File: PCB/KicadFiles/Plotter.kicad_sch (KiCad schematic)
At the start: 0 parts

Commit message: TMC2209 in Kicad
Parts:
- added U1: TMC2209-V1.2_Bigtreetech, Footprints:TMC2209-V1.2 Bigtreetech, symbol Symbols:TMC2209-V1.2_Bigtreetech
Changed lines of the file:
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@@
 (kicad_sch (version 20211123) (generator eeschema)
   (paper "A4")
+  (symbol (lib_id "Symbols:TMC2209-V1.2_Bigtreetech") (at 121.92 92.71 0) (unit 1)
+    (in_bom yes) (on_board yes) (fields_autoplaced)
+    (property "Reference" "U1" (id 0) (at 88.9 110.4899 0)
+      (effects (font (size 1.27 1.27)) (justify left))
+    )
+    (property "Value" "TMC2209-V1.2_Bigtreetech" (id 1) (at 88.9 113.0299 0)
+      (effects (font (size 1.27 1.27)) (justify left))
+    )
+    (property "Footprint" "Footprints:TMC2209-V1.2 Bigtreetech" (id 2) (at 87.63 78.74 0)
+      (effects (font (size 1.27 1.27)) hide)
+    )
+    (property "Datasheet" "https://github.com/bigtreetech/BIGTREETECH-TMC2209-V1.2/raw/master/Schematic/TMC2209-V1.2.pdf" (id 3) (at 92.71 67.31 0)
+      (effects (font (size 1.27 1.27)) hide)
+    )
+    (pin "1")
+    (pin "10")
+    (pin "11")
+    (pin "12")
+    (pin "13")
+    (pin "14")
+    (pin "15")
+    (pin "16")
+    (pin "17")
+    (pin "18")
+    (pin "2")
+    (pin "3")
+    (pin "4")
+    (pin "5")
+    (pin "6")
+    (pin "7")
+    (pin "8")
+    (pin "9")
+  )
   (sheet_instances
     (path "/" (page "1"))
   )
+  (symbol_instances
+    (path "/55d733b0-46c3-4709-8233-5c6162cfaae5"
+      (reference "U1") (unit 1) (value "TMC2209-V1.2_Bigtreetech") (footprint "Footprints:TMC2209-V1.2 Bigtreetech")
+    )
+  )
 )

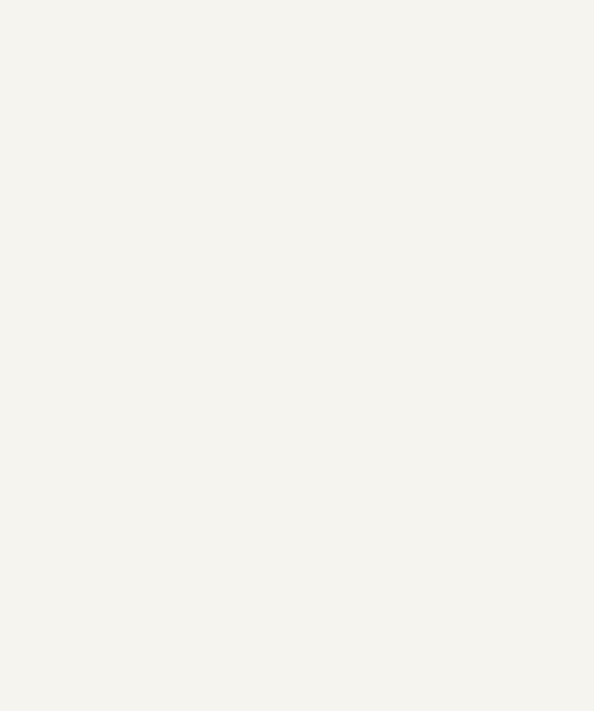
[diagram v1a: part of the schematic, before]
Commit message: stall detect lauft
https://github.com/teemuatlut/TMCStepper/issues/178
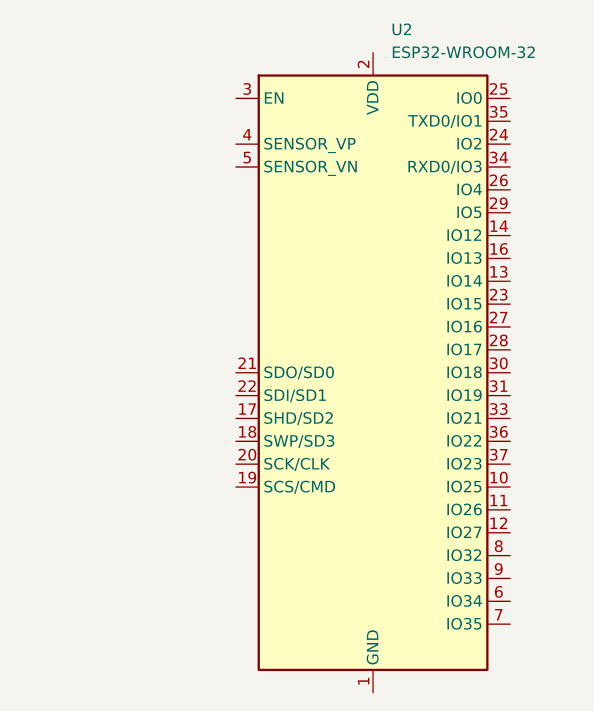
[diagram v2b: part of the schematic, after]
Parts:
- added U2: ESP32-WROOM-32, RF_Module:ESP32-WROOM-32, symbol RF_Module:ESP32-WROOM-32
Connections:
- new net: U2.1 (GND), U2.15 (GND), U2.38 (GND), U2.39 (GND)
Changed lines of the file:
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@@
+    (pin "9")
+  )
+  (symbol (lib_id "RF_Module:ESP32-WROOM-32") (at 176.53 106.68 0) (unit 1)
+    (in_bom yes) (on_board yes) (fields_autoplaced)
+    (property "Reference" "U2" (id 0) (at 178.5494 68.58 0)
+      (effects (font (size 1.27 1.27)) (justify left))
+    )
+    (property "Value" "ESP32-WROOM-32" (id 1) (at 178.5494 71.12 0)
+      (effects (font (size 1.27 1.27)) (justify left))
+    )
+    (property "Footprint" "RF_Module:ESP32-WROOM-32" (id 2) (at 176.53 144.78 0)
+      (effects (font (size 1.27 1.27)) hide)
+    )
+    (property "Datasheet" "https://www.espressif.com/sites/default/files/documentation/esp32-wroom-32_datasheet_en.pdf" (id 3) (at 168.91 105.41 0)
+      (effects (font (size 1.27 1.27)) hide)
+    )
+    (pin "1")
+    (pin "10")
+    (pin "11")
+    (pin "12")
+    (pin "13")
+    (pin "14")
+    (pin "15")
+    (pin "16")
+    (pin "17")
+    (pin "18")
+    (pin "19")
+    (pin "2")
+    (pin "20")
+    (pin "21")
+    (pin "22")
+    (pin "23")
+    (pin "24")
+    (pin "25")
+    (pin "26")
+    (pin "27")
+    (pin "28")
+    (pin "29")
+    (pin "3")
+    (pin "30")
+    (pin "31")
+    (pin "32")
+    (pin "33")
+    (pin "34")
+    (pin "35")
+    (pin "36")
+    (pin "37")
+    (pin "38")
+    (pin "39")
+    (pin "4")
+    (pin "5")
+    (pin "6")
+    (pin "7")
+    (pin "8")
     (pin "9")
   )
@@
       (reference "U1") (unit 1) (value "TMC2209-V1.2_Bigtreetech") (footprint "Footprints:TMC2209-V1.2 Bigtreetech")
     )
+    (path "/824942d7-4ef1-44b4-bd5a-14c81b4cd561"
+      (reference "U2") (unit 1) (value "ESP32-WROOM-32") (footprint "RF_Module:ESP32-WROOM-32")
+    )
   )

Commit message: schematic half way done
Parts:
- removed U1: TMC2209-V1.2_Bigtreetech, Footprints:TMC2209-V1.2 Bigtreetech, symbol Symbols:TMC2209-V1.2_Bigtreetech
- added C1, C2, C3, C6: 100u, Capacitor_SMD:CP_Elec_6.3x7.7, symbol Device:C_Polarized
- added C4, C5: C, Capacitor_SMD:C_0603_1608Metric, symbol Device:C
- added D1, D3, D4, D5: LED, LED_SMD:LED_0603_1608Metric, symbol Device:LED
- added D2: 10v, Package_TO_SOT_SMD:SOT-23, symbol Diode:BZX84Cxx
- added F1: Fuse, Fuse:Fuseholder_Cylinder-5x20mm_Schurter_0031_8201_Horizontal_Open, symbol Device:Fuse
- added H1, H2, H3, H4: MountingHole M3, MountingHole:MountingHole_3.2mm_M3_Pad_Via, symbol Mechanical:MountingHole_Pad
- added J1: JTAG, Connector_IDC:IDC-Header_2x10_P2.54mm_Vertical, symbol Connector_Generic:Conn_02x10_Odd_Even
- added J2: DBG_UART, Connector_JST:JST_XH_B3B-XH-A_1x03_P2.50mm_Vertical, symbol Connector_Generic:Conn_01x03
- added J3: 12V IN, Connector_BarrelJack:BarrelJack_CLIFF_FC681465S_SMT_Horizontal, symbol Connector:Barrel_Jack_Switch
- added J4: Motor LIN, Connector_JST:JST_XH_B4B-XH-A_1x04_P2.50mm_Vertical, symbol Connector_Generic:Conn_01x04
- added J5: Servo, Connector_JST:JST_XH_B3B-XH-A_1x03_P2.50mm_Vertical, symbol Connector_Generic:Conn_01x03
- added J6: Motor ROT, Connector_JST:JST_XH_B4B-XH-A_1x04_P2.50mm_Vertical, symbol Connector_Generic:Conn_01x04
- added Q1: SQJ479EP, Package_TO_SOT_SMD:TDSON-8-1, symbol Transistor_FET:Si7141DP
- added R1, R2, R3, R4, R5, R6, R7: 100, Resistor_SMD:R_0603_1608Metric, symbol Device:R
- added R10, R11, R12, R13, R15, R16, R18, R19, R9: 10k, Resistor_SMD:R_0603_1608Metric, symbol Device:R
- added R14, R17, R20, R8: R, Resistor_SMD:R_0603_1608Metric, symbol Device:R
- added SW1, SW2, SW3, SW4: SW_Push, Button_Switch_THT:SW_PUSH_6mm_H5mm, symbol Switch:SW_Push
- added TP1: +12V, TestPoint:TestPoint_Loop_D2.54mm_Drill1.5mm_Beaded, symbol Connector:TestPoint
- added TP2: +5V, TestPoint:TestPoint_Loop_D2.54mm_Drill1.5mm_Beaded, symbol Connector:TestPoint
- added TP3: +3.3V, TestPoint:TestPoint_Loop_D2.54mm_Drill1.5mm_Beaded, symbol Connector:TestPoint
- added U2, U5: TMC2209-V1.2_Bigtreetech, Footprints:TMC2209-V1.2 Bigtreetech, symbol Symbols:TMC2209-V1.2_Bigtreetech
- added U3: AMS1117-3.3, Package_TO_SOT_SMD:SOT-223-3_TabPin2, symbol Regulator_Linear:AMS1117-3.3
- added U4: TSR_1-2450, Converter_DCDC:Converter_DCDC_TRACO_TSR-1_THT, symbol Regulator_Switching:TSR_1-2450
- renumbered U2 to U1
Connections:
- net GND: now reaches U1.1 (GND), U1.15 (GND), U1.38 (GND), U1.39 (GND)
- net GND: now also C1.2, C2.2, C3.2, C4.2, C5.2, C6.2, D3.1 (K), D4.1 (K), D5.1 (K), H1.1, H2.1, H3.1, H4.1, J1.10 (Pin_10), J1.12 (Pin_12), J1.14 (Pin_14), J1.16 (Pin_16), J1.18 (Pin_18), J1.20 (Pin_20), J1.4 (Pin_4), J1.6 (Pin_6), J1.8 (Pin_8), J2.1 (Pin_1), J3.2, J3.3, R10.2, R12.2, R13.2, R16.2, R19.2, U2.15 (GND), U2.9 (GND), U3.1 (GND), U4.2 (GND), U5.15 (GND), U5.9 (GND)
- net TMS: now reaches U1.13 (IO14)
- net TMS: now also R3.1
- net TDI: now reaches U1.14 (IO12)
- net TDI: now also R2.1
- net TCK: now reaches U1.16 (IO13)
- net TCK: now also R4.1
- net +3.3V: now reaches U1.2 (VDD)
- net +3.3V: now also C5.1, C6.1, J1.1 (Pin_1), R11.1, R15.1, R17.1, R18.1, R9.1, TP3.1, U2.10 (VDD), U3.2 (VO), U5.10 (VDD)
- net TDO: now reaches U1.23 (IO15)
- net TDO: now also R5.1
- net CE: now reaches U1.26 (IO4)
- net MOT_UART_TX: now reaches U1.27 (IO16)
- net MOT_UART_RX: now reaches U1.28 (IO17)
- net SCK: now reaches U1.29 (IO5)
- net MOSI: now reaches U1.30 (IO18)
- net MISO: now reaches U1.31 (IO19)
- net Servo: now reaches U1.33 (IO21)
- net DEBUG_UART_RX: now reaches U1.34 (RXD0/IO3)
- net DEBUG_UART_RX: now also R7.1
- net DEBUG_UART_TX: now reaches U1.35 (TXD0/IO1)
- net DEBUG_UART_TX: now also R6.1
- net SCL: now reaches U1.36 (IO22)
- net SDA: now reaches U1.37 (IO23)
- new net: R15.2, R16.1, U5.2 (MS1)
- new net: J1.7 (Pin_7), R3.2
- new net: R11.2, R12.1, U2.3 (MS2)
- new net: J6.4 (Pin_4), U5.11 (B2)
- new net: J6.3 (Pin_3), U5.12 (B1)
- new net: J6.2 (Pin_2), U5.13 (A1)
- new net: J6.1 (Pin_1), U5.14 (A2)
- new net: R18.2, R19.1, U5.3 (MS2)
- new net: J2.2 (Pin_2), R7.2
- new net: J2.3 (Pin_3), R6.2
- new net: F1.1, J3.1
- new net: D4.2 (A), R17.2
- new net: D2.1 (A), Q1.4 (G), R13.1
- new net: J4.1 (Pin_1), U2.14 (A2)
- new net: J4.2 (Pin_2), U2.13 (A1)
- new net: J4.3 (Pin_3), U2.12 (B1)
- new net: J4.4 (Pin_4), U2.11 (B2)
- new net: J1.13 (Pin_13), R5.2
- new net: J1.3 (Pin_3), R1.2
- new net: J1.5 (Pin_5), R2.2
- new net: J1.9 (Pin_9), R4.2
- new net: D3.2 (A), R14.2
- new net: R10.1, R9.2, U2.2 (MS1)
- new net: D5.2 (A), R20.2
- new net: F1.2, Q1.5 (D)
- new net +12V: C1.1, C3.1, D2.3 (K), Q1.1 (S), Q1.2 (S), Q1.3 (S), R20.1, TP1.1, U2.16 (VM), U4.1 (Vin), U5.16 (VM)
- new net +5V: C2.1, C4.1, R14.1, TP2.1, U3.3 (VI), U4.3 (Vout)
- new net MOT_EN: U2.1 (EN), U5.1 (EN)
- new net MOT_LIN_DIAG: U2.17 (DIAG)
- new net MOT_LIN_DIR: U2.8 (DIR)
- new net MOT_LIN_STEP: U2.7 (STEP)
- new net MOT_ROT_DIAG: U5.17 (DIAG)
- new net MOT_ROT_DIR: U5.8 (DIR)
- new net MOT_ROT_STEP: U5.7 (STEP)
- new net MOT_UART: U2.4 (PDN), U2.5 (PDN), U5.4 (PDN), U5.5 (PDN)
- new net RST: R1.1
- no-connect marks 0 -> 15
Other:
- note added: "Debug UART Interface"
- note added: "JTAG Interface"
- note added: "Microcontroller"
- note added: "Motor Drivers"
- note added: "Mounting Holes"
- note added: "Power Supply"
- company: (none) -> Lorenz Geisser
- title: (none) -> Plotter
- moved on the sheet: U1

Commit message: finished schematic
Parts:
- removed D1: LED, LED_SMD:LED_0603_1608Metric, symbol Device:LED
- removed SW1, SW2: SW_Push, Button_Switch_THT:SW_PUSH_6mm_H5mm, symbol Switch:SW_Push
- added C5, C6, C7, C8: 100n, Capacitor_SMD:C_0603_1608Metric, symbol Device:C
- added R17, R22, R24, R26, R28, R5: 1k, Resistor_SMD:R_0603_1608Metric, symbol Device:R
- added R18, R19, R20, R21: 100, Resistor_SMD:R_0603_1608Metric, symbol Device:R
- added R23, R25, R27, R29, R6, R7: 10k, Resistor_SMD:R_0603_1608Metric, symbol Device:R
- added R9: 3k, Resistor_SMD:R_0603_1608Metric, symbol Device:R
- added SW3: Enter, Button_Switch_THT:SW_PUSH_6mm_H5mm, symbol Switch:SW_Push
- added SW4: RST, Button_Switch_THT:SW_PUSH_6mm_H5mm, symbol Switch:SW_Push
- added U4: MicroSD, Footprints:GCT-MEM2055-00-190-01-A, symbol Symbols:MicroSD_SPI_CD
- added U5: OLED_Display, Footprints:Display_128x64_096_I2C, symbol Symbols:Oled
- R8: value R -> 3k
- SW1: renamed from SW4; value SW_Push -> Down
- SW2: renamed from SW3; value SW_Push -> Up
- renumbered C2 to C1, C3 to C10, C4 to C2, C5 to C3, C6 to C4, C1 to C9, D2 to D1, D5 to D2, J3 to J1, J1 to J2, J2 to J3, J5 to J4, J4 to J5, R13 to R1, R1 to R10, R2 to R11, R3 to R12, R4 to R13, R5 to R14, R6 to R15, R7 to R16, R20 to R2, R14 to R3, R9 to R30, R10 to R31, R15 to R32, R16 to R33, R11 to R34, R12 to R35, R18 to R36, R19 to R37, R17 to R4, U4 to U1, U3 to U2, U1 to U3, U2 to U6, U5 to U7
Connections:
- net MOT_UART_TX is gone; now on net MOT_UART: U3.27 (IO16)
- net +3.3V: now also R8.1, R23.1, R25.1, R27.1, R29.1, R6.1, R9.1, U4.4 (VDD), U5.2 (VCC)
- net +5V: now also J4.2 (Pin_2)
- net GND: now also J4.1 (Pin_1), SW1.1, SW2.1, C5.2, C6.2, C7.2, C8.2, R7.2, SW3.1, SW4.1, U4.10 (Schield), U4.6 (GND), U5.1 (GND)
- net MOT_EN: now also U3.7 (IO35)
- net MOT_LIN_DIAG: now also U3.11 (IO26)
- net MOT_LIN_DIR: now also U3.8 (IO32)
- net MOT_LIN_STEP: now also U3.12 (IO27)
- net MOT_ROT_DIAG: now also U3.10 (IO25)
- net MOT_ROT_DIR: now also U3.6 (IO34)
- net MOT_ROT_STEP: now also U3.9 (IO33)
- net MOT_UART: now also R5.1
- net RST: now also U3.3 (EN), C8.1, R28.2, R29.2
- net SCL: now also R9.2, U5.3 (SCL)
- net SDA: now also R8.2, U5.4 (SDA)
- net Servo: now also R17.1
- net at SW1.2: now also R22.1
- net SW_Down: now reaches U3.24 (IO2)
- net SW_Down: now also C5.1, R22.2, R23.2
- net at U3.25 (IO0): now also R6.2, R7.1
- net SW_Up: now reaches U3.4 (SENSOR_VP)
- net SW_Up: now also C6.1, R24.2, R25.2
- net SW_Enter: now reaches U3.5 (SENSOR_VN)
- net SW_Enter: now also C7.1, R26.2, R27.2
- net at SW2.2: now also R24.1
- net at J4.3 (Pin_3): now also R17.2
- net CE renamed SD_CE
- net SD_CE: now also R18.1
- net MISO renamed SD_MISO
- net SD_MISO: now also R21.1
- net MOSI renamed SD_MOSI
- net SD_MOSI: now also R19.1
- net MOT_UART_RX: no longer names the net of U3.28 (IO17)
- net MOT_UART_RX: now also R5.2
- net SCK renamed SD_SCK
- net SD_SCK: now also R20.1
- net TCK renamed JTAG_TCK
- net TDI renamed JTAG_TDI
- net TDO renamed JTAG_TDO
- net TMS renamed JTAG_TMS
- new net: R19.2, U4.3 (DI)
- new net: R21.2, U4.7 (DO)
- new net: R18.2, U4.2 (~{CS})
- new net: R28.1, SW4.2
- new net: R20.2, U4.5 (SCLK)
- new net: R26.1, SW3.2
- no-connect marks 15 -> 18
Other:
- note added: "SD Card Interface"
- note added: "Servo Output"
- note added: "User Interface"
- moved on the sheet: J2, J4, R10, R11, R12, R13, R14, SW1, SW2, U3

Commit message: stm32??
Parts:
- added C? (x2): C, symbol Device:C
- added C? (x4): 100n, Capacitor_SMD:C_0805_2012Metric, symbol Device:C
- added JP1: SolderJumper_3_Open, Jumper:SolderJumper-3_P1.3mm_Open_RoundedPad1.0x1.5mm, symbol Jumper:SolderJumper_3_Open
- added R? (x2): 10k, Resistor_SMD:R_0805_2012Metric, symbol Device:R
- added U8: STM32F411CEU6, Package_DFN_QFN:QFN-48-1EP_7x7mm_P0.5mm_EP5.6x5.6mm, symbol MCU_ST_STM32F4:STM32F411CEUx
- added Y?: 25MHz, symbol Device:Crystal_GND23
- C2, C3, C5, C6, C7, C8: footprint Capacitor_SMD:C_0603_1608Metric -> Capacitor_SMD:C_0805_2012Metric
- D2, D3, D4: footprint LED_SMD:LED_0603_1608Metric -> LED_SMD:LED_0805_2012Metric
- R1, R10, R11, R12, R13, R14, R15, R16, R17, R18, R19, R2, R20, R21, R22, R23, R24, R25, R26, R27, R28, R29, R3, R30, R31, R32, R33, R34, R35, R36, R37, R4, R5, R6, R7, R8, R9: footprint Resistor_SMD:R_0603_1608Metric -> Resistor_SMD:R_0805_2012Metric
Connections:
- net +3.3V: now also C?.1, C?.1, C?.1, C?.1, U8.1 (VBAT), U8.24 (VDD), U8.36 (VDD), U8.48 (VDD), U8.9 (VDDA)
- net GND: now also C?.2, C?.2, C?.2, C?.2, C?.2, C?.2, R?.1, R?.1, U8.23 (VSS), U8.35 (VSS), U8.47 (VSS), U8.49 (VSS), U8.8 (VSSA), Y?.2, Y?.3
- new net: C?.1, Y?.4
- new net: R?.2, U8.20 (PB2)
- new net: C?.1, Y?.1
- new net: R?.2, U8.44 (BOOT0)
- no-connect marks 18 -> 20

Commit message: bald fertig
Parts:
- removed J1: 12V IN, Connector_BarrelJack:BarrelJack_CLIFF_FC681465S_SMT_Horizontal, symbol Connector:Barrel_Jack_Switch
- removed J3: DBG_UART, Connector_JST:JST_XH_B3B-XH-A_1x03_P2.50mm_Vertical, symbol Connector_Generic:Conn_01x03
- removed R15, R16: 100, Resistor_SMD:R_0805_2012Metric, symbol Device:R
- removed R30, R31, R32, R33, R34, R35, R36, R37: 10k, Resistor_SMD:R_0805_2012Metric, symbol Device:R
- removed R5: 1k, Resistor_SMD:R_0805_2012Metric, symbol Device:R
- removed R8: 3k, Resistor_SMD:R_0805_2012Metric, symbol Device:R
- removed TP1: +12V, TestPoint:TestPoint_Loop_D2.54mm_Drill1.5mm_Beaded, symbol Connector:TestPoint
- removed TP2: +5V, TestPoint:TestPoint_Loop_D2.54mm_Drill1.5mm_Beaded, symbol Connector:TestPoint
- removed TP3: +3.3V, TestPoint:TestPoint_Loop_D2.54mm_Drill1.5mm_Beaded, symbol Connector:TestPoint
- removed U3: ESP32-WROOM-32, RF_Module:ESP32-WROOM-32, symbol RF_Module:ESP32-WROOM-32
- removed U8: STM32F411CEU6, Package_DFN_QFN:QFN-48-1EP_7x7mm_P0.5mm_EP5.6x5.6mm, symbol MCU_ST_STM32F4:STM32F411CEUx
- removed Y?: 25MHz, symbol Device:Crystal_GND23
- added C16: 100n, Capacitor_SMD:C_0805_2012Metric, symbol Device:C
- added C5: 2.2u, Capacitor_SMD:C_0402_1005Metric, symbol Device:C
- added D5: Status, LED_SMD:LED_0805_2012Metric, symbol Device:LED
- added J1: 12V Input, Connector_JST:JST_XH_B2B-XH-A_1x02_P2.50mm_Vertical, symbol Connector_Generic:Conn_01x02
- added J4: Ext. Switch, Connector_JST:JST_XH_B2B-XH-A_1x02_P2.50mm_Vertical, symbol Connector_Generic:Conn_01x02
- added JP2: Y_MS1, Jumper:SolderJumper-3_P1.3mm_Open_RoundedPad1.0x1.5mm, symbol Jumper:SolderJumper_3_Open
- added JP3: X_MS2, Jumper:SolderJumper-3_P1.3mm_Open_RoundedPad1.0x1.5mm, symbol Jumper:SolderJumper_3_Open
- added JP4: Y_MS2, Jumper:SolderJumper-3_P1.3mm_Open_RoundedPad1.0x1.5mm, symbol Jumper:SolderJumper_3_Open
- added R24: 10k, Resistor_SMD:R_0805_2012Metric, symbol Device:R
- added R28: 100, Resistor_SMD:R_0805_2012Metric, symbol Device:R
- added U3: STM32F411CEU&, Package_DFN_QFN:QFN-48-1EP_7x7mm_P0.5mm_EP5.6x5.6mm, symbol Symbols:STM32F411CEUx
- added Y1: 25MHz, Crystal:Crystal_SMD_3225-4Pin_3.2x2.5mm, symbol Device:Crystal_GND24
- C10, C11: renamed from C?; value C -> 12p; footprint (none) -> Capacitor_SMD:C_0402_1005Metric
- C2, C3: value C -> 10u
- C6, C7, C8, C9: renamed from C?; footprint Capacitor_SMD:C_0805_2012Metric -> Capacitor_SMD:C_0402_1005Metric
- D2: value LED -> 12V
- D3: value LED -> 5V
- D4: value LED -> 3.3V
- J5: value Motor LIN -> Motor X
- J6: value Motor ROT -> Motor Y
- JP1: value SolderJumper_3_Open -> X_MS1
- R10: value 100 -> 1k
- R2, R3, R4: value R -> 1k
- R23: renamed from R17; value 1k -> 100
- R6, R7: value 10k -> 3k
- R9: value 3k -> 1k
- SW3: value Enter -> OK
- gave numbers to parts that had none: 2
- renumbered C5 to C12, C6 to C13, C7 to C14, C8 to C15, C9 to C17, C10 to C18, J4 to J3, R22 to R11, R23 to R12, R24 to R13, R25 to R14, R26 to R15, R27 to R16, R28 to R17, R29 to R18, R13 to R19, R11 to R20, R12 to R21, R14 to R22, R18 to R25, R19 to R26, R20 to R27, R21 to R29, U5 to U4, U4 to U5
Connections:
- net +3.3V: now also JP1.3 (B), R7.1, JP2.3 (B), JP3.3 (B), JP4.3 (B), R24.2, U3.1 (VBAT), U3.24 (VDD), U3.36 (VDD), U3.48 (VDD), U3.9 (VDDA); no longer R9.1
- net +5V: now also C16.1
- net GND: now also JP1.1 (A), C16.2, C5.2, D5.1 (K), J1.1 (Pin_1), J4.1 (Pin_1), JP2.1 (A), JP3.1 (A), JP4.1 (A), U3.23 (VSS), U3.35 (VSS), U3.47 (VSS), U3.49 (VSS), U3.8 (VSSA), Y1.2, Y1.4; no longer R7.2
- net MOT_EN: now also U3.17 (PA7)
- net MOT_UART: now also R10.2, U3.13 (PA3)
- net RST: now also U3.7 (NRST); no longer R10.1
- net SD_CE: now also U3.39 (PB3)
- net SD_MISO: now also U3.32 (PA11)
- net SD_MOSI: now also U3.11 (PA1)
- net SD_SCK: now also U3.26 (PB13)
- net SW_Down: now also U3.40 (PB4)
- net SW_Up: now also U3.45 (PB8)
- net Servo: now also U3.29 (PA8)
- net at C10.1: now also U3.5 (PH0), Y1.1
- net at U7.2 (MS1): now also JP2.2 (C)
- net at R21.2: now also J2.9 (Pin_9); no longer J2.7 (Pin_7)
- net at U6.3 (MS2): now also JP3.2 (C)
- net at U7.3 (MS2): now also JP4.2 (C)
- net at R8.2: now also U3.20 (PB2)
- net at C11.1: now also U3.6 (PH1), Y1.3
- net at F1.1: now also J1.2 (Pin_2)
- net at R5.2: now also U3.44 (BOOT0)
- net at J2.13 (Pin_13): no longer R22.2
- net at J2.17 (Pin_17): now also R22.2
- net at J2.3 (Pin_3): no longer R10.2
- net at J2.5 (Pin_5): now also R19.2; no longer R20.2
- net I2C_SCL: now reaches R6.2
- net I2C_SCL: now also U4.3 (SCL), U3.42 (PB6); no longer R7.1
- net at U6.2 (MS1): now also JP1.2 (C)
- net at U5.9 (CD): now also R28.2
- net JTAG_TCK renamed PC_UART_RX
- net PC_UART_RX: now also U3.31 (PA10)
- net JTAG_TDI renamed SWD_SWDIO
- net SWD_SWDIO: now also U3.34 (PA13)
- net JTAG_TDO renamed PC_UART_TX
- net PC_UART_TX: now also U3.30 (PA9)
- net JTAG_TMS renamed SWD_SWCLK
- net SWD_SWCLK: now also U3.37 (PA14)
- net MOT_LIN_DIAG renamed MOT_X_DIAG
- net MOT_X_DIAG: now also U3.18 (PB0)
- net MOT_LIN_DIR renamed MOT_X_DIR
- net MOT_X_DIR: now also U3.15 (PA5)
- net MOT_LIN_STEP renamed MOT_X_STEP
- net MOT_X_STEP: now also U3.16 (PA6)
- net MOT_ROT_DIAG renamed MOT_Y_DIAG
- net MOT_Y_DIAG: now also U3.28 (PB15)
- net MOT_ROT_DIR renamed MOT_Y_DIR
- net MOT_Y_DIR: now also U3.25 (PB12)
- net MOT_ROT_STEP renamed MOT_Y_STEP
- net MOT_Y_STEP: now also U3.27 (PB14)
- net SCL: no longer names the net of R9.2
- net SCL: now also U3.2 (PC13); no longer U4.3 (SCL)
- net SDA renamed I2C_SDA
- net I2C_SDA: now also R7.2, U3.43 (PB7)
- net SW_Enter renamed SW_OK
- net SW_OK: now also U3.41 (PB5)
- new net: D5.2 (A), R9.1
- new net: J2.7 (Pin_7), R20.2
- new net: R10.1, U3.12 (PA2)
- new net: C5.1, U3.22 (VCAP1)
- new net Ext. Switch: J4.2 (Pin_2), R24.1, U3.14 (PA4)
- new net SD_DETECT: R28.1, U3.38 (PA15)
- no-connect marks 20 -> 18
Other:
- note added: "<"
- note added: ">"
- note added: "Ext. Switch Input"
- note added: "SWD / UART Interface"
- note removed: "Debug UART Interface"
- note removed: "JTAG Interface"
- moved on the sheet: C1, C10, C11, C13, C14, C15, C17, C18, C2, C4, C6, C7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
